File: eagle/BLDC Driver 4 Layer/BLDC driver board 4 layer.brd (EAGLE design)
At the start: 38 parts, among them Q1 CSD173XXQX-NEXFET, Q11 CSD173XXQX-NEXFET, Q3 CSD173XXQX-NEXFET, Q5 CSD173XXQX-NEXFET, Q7 CSD173XXQX-NEXFET, Q9 CSD173XXQX-NEXFET

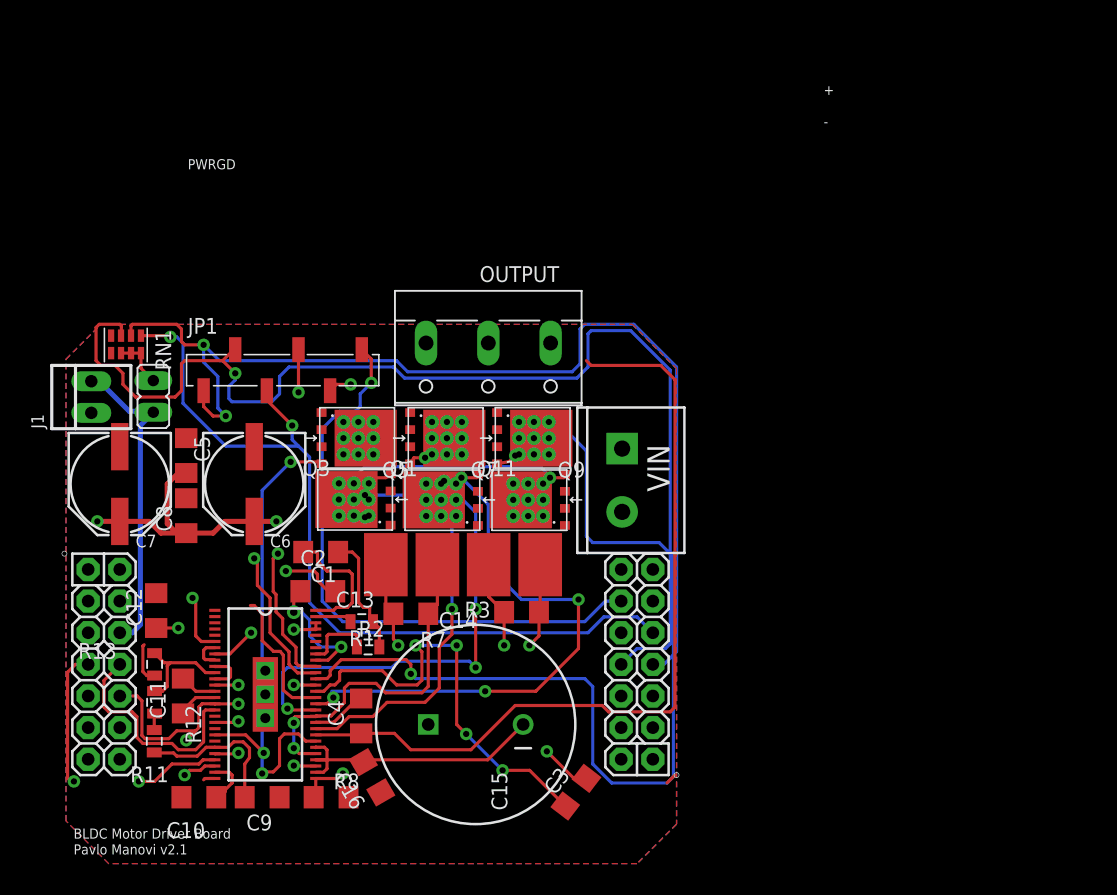
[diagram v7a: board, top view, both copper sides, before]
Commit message: exploded 4-layer bldc due to space boon
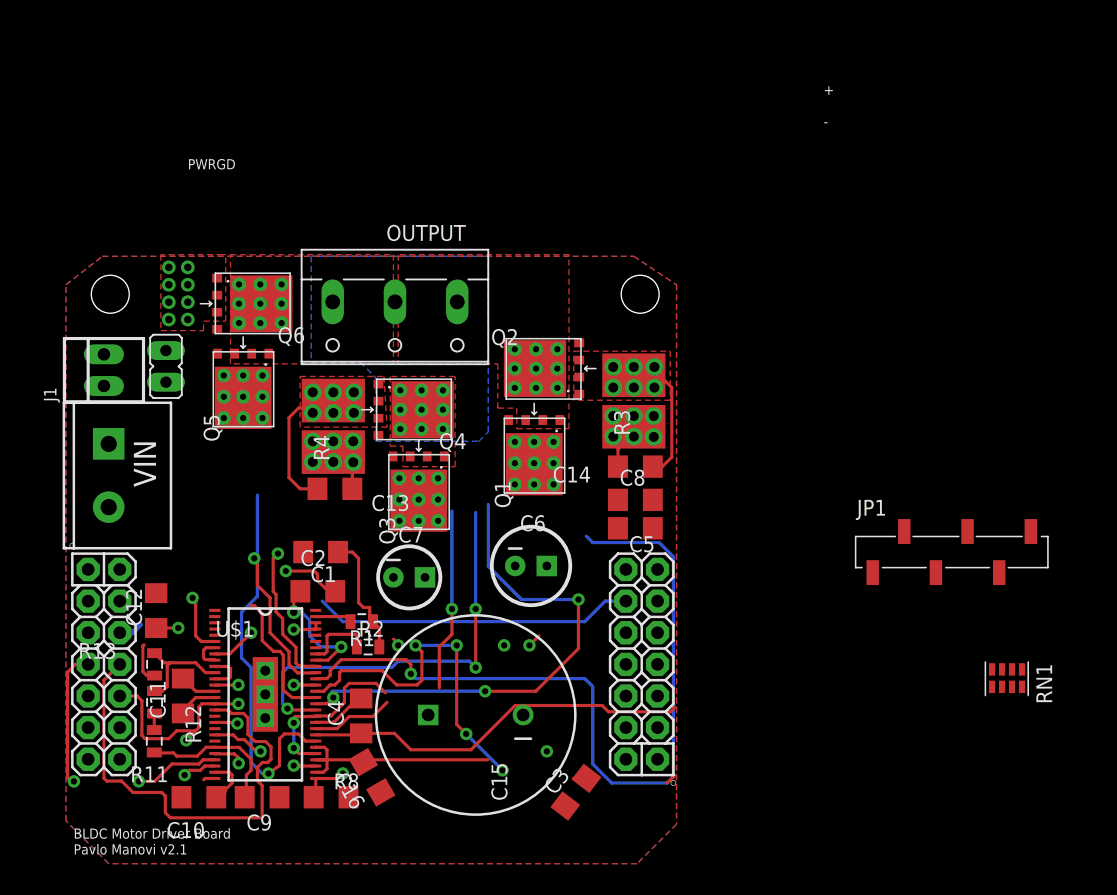
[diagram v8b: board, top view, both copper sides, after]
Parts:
- removed Q11, Q7, Q9: CSD173XXQX-NEXFET, pavlo:CSD173XXQX
- removed R7: .01, pavlo:SMT-REF
- added E$1, E$2: (no value), ASL:STAND-OFF-TIGHT
- added Q2, Q4, Q6: CSD173XXQX-NEXFET, pavlo:CSD173XXQX
- added R4: .01, pavlo:SMT-REF
- C6: device ASL:PANASONIC_E -> pavlo:CPOL-RADIAL-6.3MM
- C7: device ASL:PANASONIC_E -> pavlo:CPOL-RADIA-5MM
- U$1: value DRV8302 -> DRV8302-56
- U$2: device ASL:CAN_NODE_SHIELD_V3 -> ASL:CANODE_SHIELD
- moved RN1 75.6 mm to (79.4, 16.1)
- moved JP1 55.7 mm to (80.1, 25.5)
- moved VIN 41.2 mm to (6.10, 31.7)
- moved C5 36.5 mm to (48.4, 27.4), turned to 0 degrees
- moved C8 36.1 mm to (48.4, 29.7), turned to 0 degrees
- moved C7 24.4 mm to (30.2, 23.5), turned to 0 degrees
- moved C6 23.1 mm to (40.0, 24.5), turned to 0 degrees
- moved R3 16.2 mm to (48.3, 37.6), turned to 90 degrees
- moved C14 14.8 mm to (48.4, 32.4)
- moved C13 11.7 mm to (24.3, 30.6), turned to 0 degrees
- moved Q5 11.2 mm to (16.9, 36.7), turned to 90 degrees
- moved Q1 9.42 mm to (40.3, 31.4), turned to 90 degrees
- moved OUTPUT 8.19 mm to (29.1, 44.3)
- moved Q3 7.13 mm to (31.0, 28.4), turned to 90 degrees
- moved JP3 2.62 mm to (10.7, 40.4)
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- renumbered DRV8301 to U$1
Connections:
- net GH_A: now also Q1.G; no longer Q11.G
- net GH_B: now also Q3.G; no longer Q1.G
- net GH_C: now also Q5.G; no longer Q3.G
- net GL_A: now also Q2.G; no longer Q9.G
- net GL_B: now also Q4.G; no longer Q7.G
- net GL_C: now also Q6.G; no longer Q5.G
- net GND: now also C6.2, C7.2; no longer C6.-, C7.-
- net OUTPUTA: now also Q1.S1, Q1.S2, Q1.S3, Q2.D, Q2.P$1, Q2.P$2, Q2.P$3, Q2.P$4, Q2.P$5, Q2.P$6, Q2.P$7, Q2.P$8, Q2.P$9; no longer Q11.S1, Q11.S2, Q11.S3, Q9.D
- net OUTPUTB: now also Q3.S1, Q3.S2, Q3.S3, Q4.D, Q4.P$1, Q4.P$2, Q4.P$3, Q4.P$4, Q4.P$5, Q4.P$6, Q4.P$7, Q4.P$8, Q4.P$9; no longer Q1.S1, Q1.S2, Q1.S3, Q7.D
- net OUTPUTC: now also Q5.S1, Q5.S2, Q5.S3, Q6.D, Q6.P$1, Q6.P$2, Q6.P$3, Q6.P$4, Q6.P$5, Q6.P$6, Q6.P$7, Q6.P$8, Q6.P$9; no longer Q3.S1, Q3.S2, Q3.S3, Q5.D
- net SN1: now also Q4.S1, Q4.S2, Q4.S3, R4.1, R4.P$10, R4.P$11, R4.P$12, R4.P$7, R4.P$8, R4.P$9; no longer Q7.S1, Q7.S2, Q7.S3, R7.2
- net SN2: now also Q2.S1, Q2.S2, Q2.S3, R3.1, R3.P$10, R3.P$11, R3.P$12, R3.P$7, R3.P$8, R3.P$9; no longer Q9.S1, Q9.S2, Q9.S3, R3.2
- net VNEG: now also Q6.S1, Q6.S2, Q6.S3, R3.2, R3.P$1, R3.P$2, R3.P$3, R3.P$4, R3.P$5, R3.P$6, R4.2, R4.P$1, R4.P$2, R4.P$3, R4.P$4, R4.P$5, R4.P$6; no longer Q5.S1, Q5.S2, Q5.S3, R3.1, R7.1
- net V_BATT: now also C6.1, C7.1, Q1.P$1, Q1.P$2, Q1.P$3, Q1.P$4, Q1.P$5, Q1.P$6, Q1.P$7, Q1.P$8, Q1.P$9, Q3.P$1, Q3.P$2, Q3.P$3, Q3.P$4, Q3.P$5, Q3.P$6, Q3.P$7, Q3.P$8, Q3.P$9, Q5.D, Q5.P$1, Q5.P$2, Q5.P$3, Q5.P$4, Q5.P$5, Q5.P$6, Q5.P$7, Q5.P$8, Q5.P$9; no longer C6.+, C7.+, Q11.D
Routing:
- net ADC/HALL2: track 94.0 -> 0.00 mm, vias 1 -> 0
- net ADC/HALL1: track 86.5 -> 0.00 mm, vias 2 -> 0
- net ADC/HALL3: track 67.2 -> 0.00 mm, vias 2 -> 0
- net QEI-A: track 49.2 -> 0.00 mm, vias 1 -> 0
- net OUTPUTA: track 58.9 -> 20.0 mm
- net OUTPUTC: track 66.2 -> 32.2 mm
- net QEI-B: track 52.7 -> 24.9 mm, vias 1 -> 0
- net GH_A: track 41.4 -> 15.5 mm, vias 3 -> 1
- net VCC: track 25.6 -> 1.91 mm
- net QEI-INDEX: track 48.3 -> 25.8 mm, vias 1 -> 0
- net V_BATT: track 28.7 -> 6.51 mm, vias 4 -> 2
- net PWM1: track 18.0 -> 37.5 mm
- net GL_A: track 79.2 -> 63.3 mm, vias 2 -> 1
- net GH_C: track 36.8 -> 21.2 mm, vias 2 -> 1
- net N$1: track 11.3 -> 0.00 mm
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- added copper zone on layer 1, net OUTPUTA
- added copper zone on layer 1, net OUTPUTB
- added copper zone on layer 16, net OUTPUTB
- added copper zone on layer 1, net OUTPUTC
- added copper zone on layer 1, net SN1
- added copper zone on layer 1, net SN2
- added copper zone on layer 1, net VNEG
